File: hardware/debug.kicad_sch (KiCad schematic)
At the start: 62 parts, among them U11 74HC244, U12 74HC244, U13 74HC244

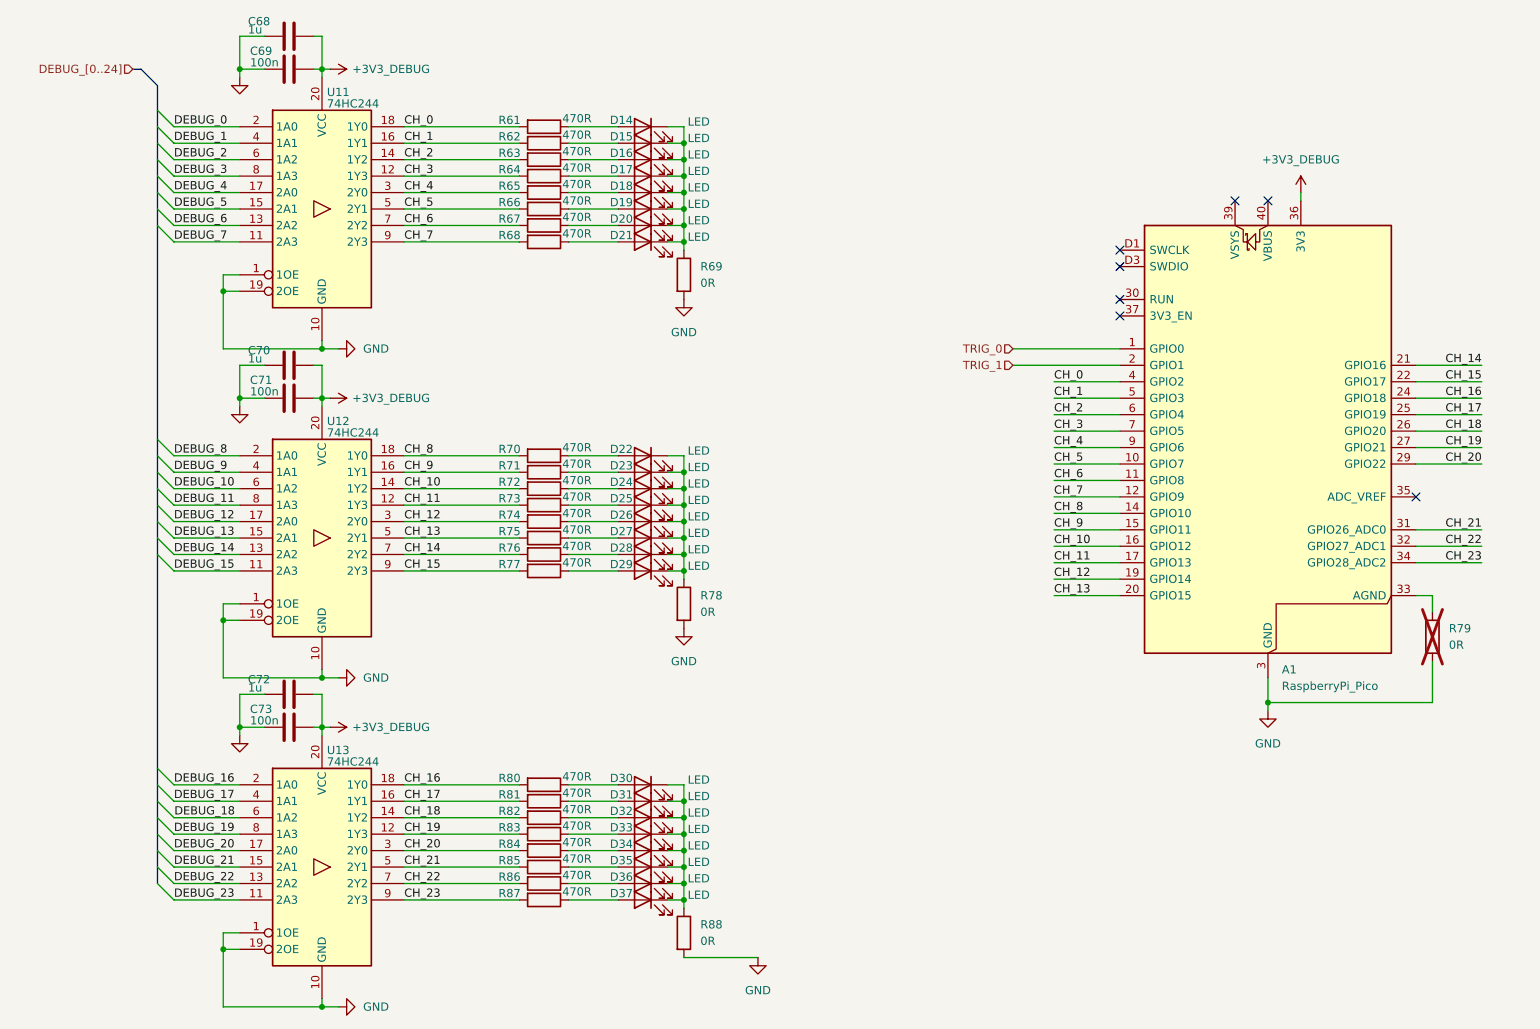
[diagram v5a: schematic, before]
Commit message: route all signal
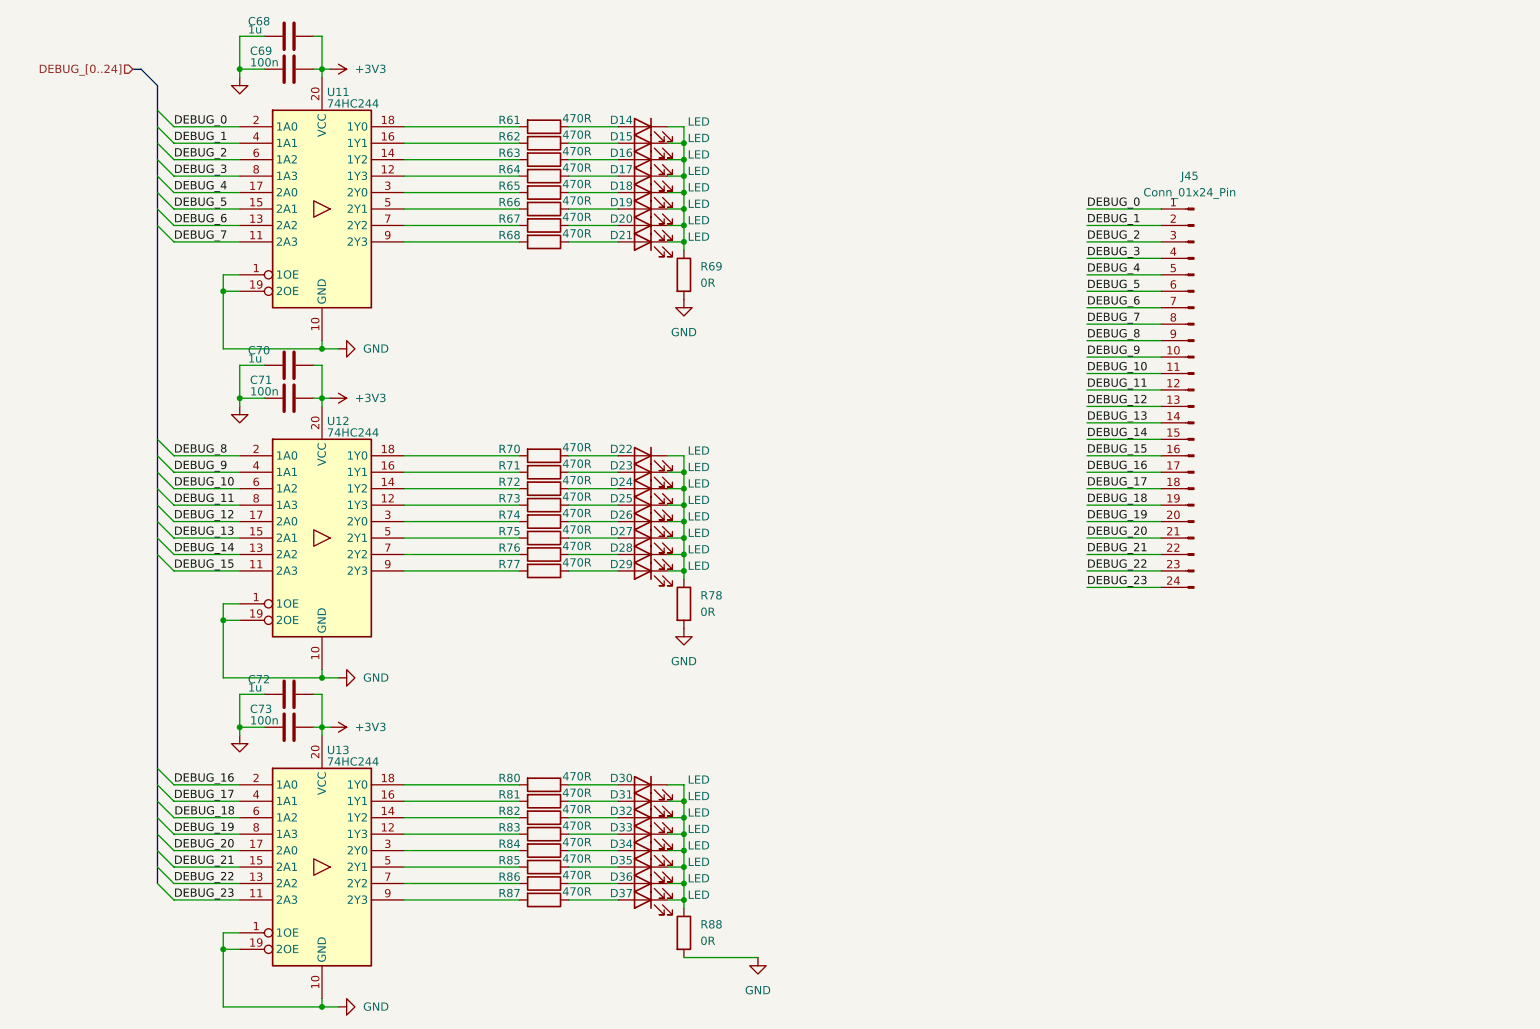
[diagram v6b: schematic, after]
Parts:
- removed A1: RaspberryPi_Pico, Module:RaspberryPi_Pico_SMD_HandSolder, symbol MCU_Module:RaspberryPi_Pico_Debug
- removed R79: 0R, Resistor_SMD:R_0402_1005Metric, symbol Device:R
- added J45: Conn_01x24_Pin, Connector_PinHeader_2.54mm:PinHeader_1x24_P2.54mm_Vertical, symbol Connector:Conn_01x24_Pin
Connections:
- net DEBUG_0: now also J45.1 (Pin_1)
- net DEBUG_1: now also J45.2 (Pin_2)
- net DEBUG_10: now also J45.11 (Pin_11)
- net DEBUG_11: now also J45.12 (Pin_12)
- net DEBUG_12: now also J45.13 (Pin_13)
- net DEBUG_13: now also J45.14 (Pin_14)
- net DEBUG_14: now also J45.15 (Pin_15)
- net DEBUG_15: now also J45.16 (Pin_16)
- net DEBUG_16: now also J45.17 (Pin_17)
- net DEBUG_17: now also J45.18 (Pin_18)
- net DEBUG_18: now also J45.19 (Pin_19)
- net DEBUG_19: now also J45.20 (Pin_20)
- net DEBUG_2: now also J45.3 (Pin_3)
- net DEBUG_20: now also J45.21 (Pin_21)
- net DEBUG_21: now also J45.22 (Pin_22)
- net DEBUG_22: now also J45.23 (Pin_23)
- net DEBUG_23: now also J45.24 (Pin_24)
- net DEBUG_3: now also J45.4 (Pin_4)
- net DEBUG_4: now also J45.5 (Pin_5)
- net DEBUG_5: now also J45.6 (Pin_6)
- net DEBUG_6: now also J45.7 (Pin_7)
- net DEBUG_7: now also J45.8 (Pin_8)
- net DEBUG_8: now also J45.9 (Pin_9)
- net DEBUG_9: now also J45.10 (Pin_10)
- net +3V3_DEBUG renamed +3V3
- net CH_0: no longer names the net of R61.2, U11.18 (1Y0)
- net CH_1: no longer names the net of R62.2, U11.16 (1Y1)
- net CH_10: no longer names the net of R72.2, U12.14 (1Y2)
- net CH_11: no longer names the net of R73.2, U12.12 (1Y3)
- net CH_12: no longer names the net of R74.2, U12.3 (2Y0)
- net CH_13: no longer names the net of R75.2, U12.5 (2Y1)
- net CH_14: no longer names the net of R76.2, U12.7 (2Y2)
- net CH_15: no longer names the net of R77.2, U12.9 (2Y3)
- net CH_16: no longer names the net of R80.2, U13.18 (1Y0)
- net CH_17: no longer names the net of R81.2, U13.16 (1Y1)
- net CH_18: no longer names the net of R82.2, U13.14 (1Y2)
- net CH_19: no longer names the net of R83.2, U13.12 (1Y3)
- net CH_2: no longer names the net of R63.2, U11.14 (1Y2)
- net CH_20: no longer names the net of R84.2, U13.3 (2Y0)
- net CH_21: no longer names the net of R85.2, U13.5 (2Y1)
- net CH_22: no longer names the net of R86.2, U13.7 (2Y2)
- net CH_23: no longer names the net of R87.2, U13.9 (2Y3)
- net CH_3: no longer names the net of R64.2, U11.12 (1Y3)
- net CH_4: no longer names the net of R65.2, U11.3 (2Y0)
- net CH_5: no longer names the net of R66.2, U11.5 (2Y1)
- net CH_6: no longer names the net of R67.2, U11.7 (2Y2)
- net CH_7: no longer names the net of R68.2, U11.9 (2Y3)
- net CH_8: no longer names the net of R70.2, U12.18 (1Y0)
- net CH_9: no longer names the net of R71.2, U12.16 (1Y1)
- no-connect marks 7 -> 0
